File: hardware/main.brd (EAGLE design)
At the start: 96.5 x 65.5 mm, 93 parts, among them SW1 USER_SLIDE, SW2 USER_SLIDE, U1 TMS320F28069_PN_80, U10 TXB0101_DBV_6, U2 SN74LVC4245A_DW_24, U3 Value, U4 SN74LVC4245A_DW_24, U5 Value, U6 SN74ABT541B_DW_20, U7 SN74LVC1G04_DBV_5, U8 SST25VF080BS2AF, U9 TXB0101_DBV_6

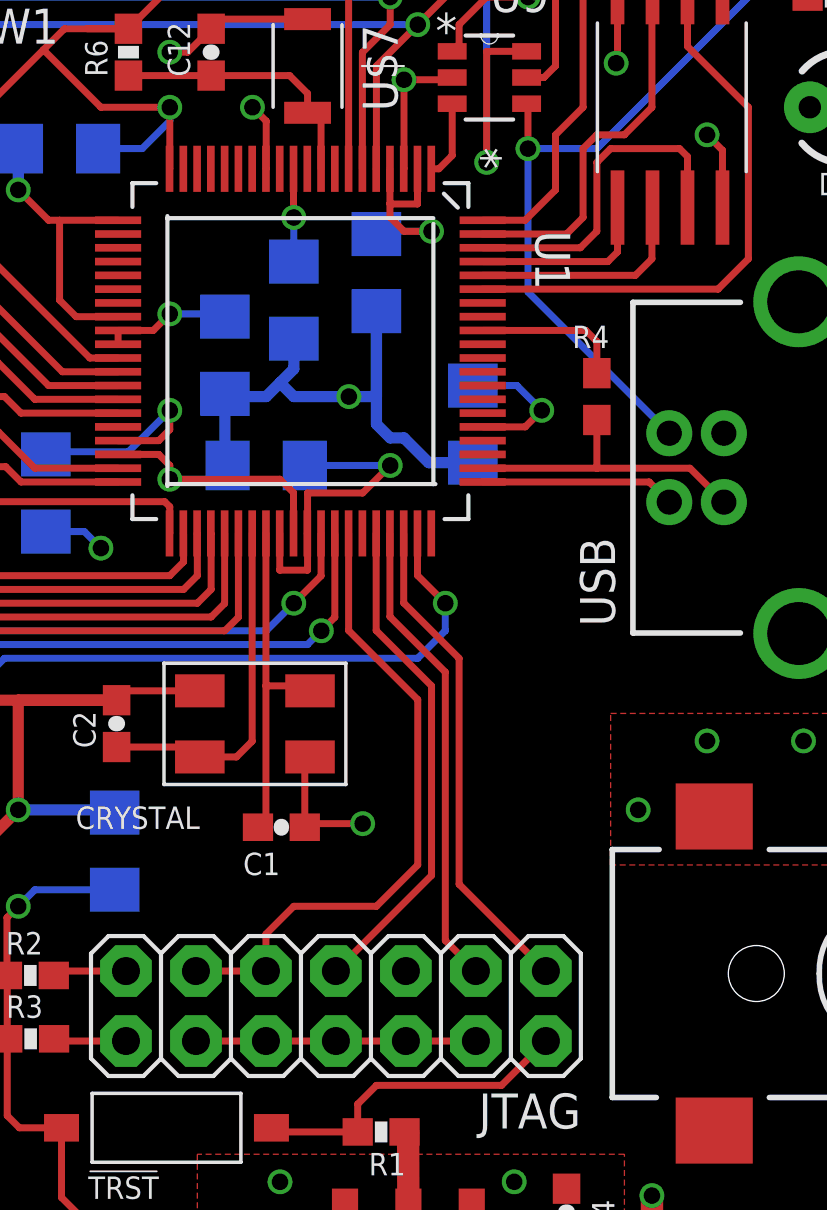
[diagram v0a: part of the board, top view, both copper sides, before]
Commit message: Fixed minor error with JTAG. TRST pin not connected
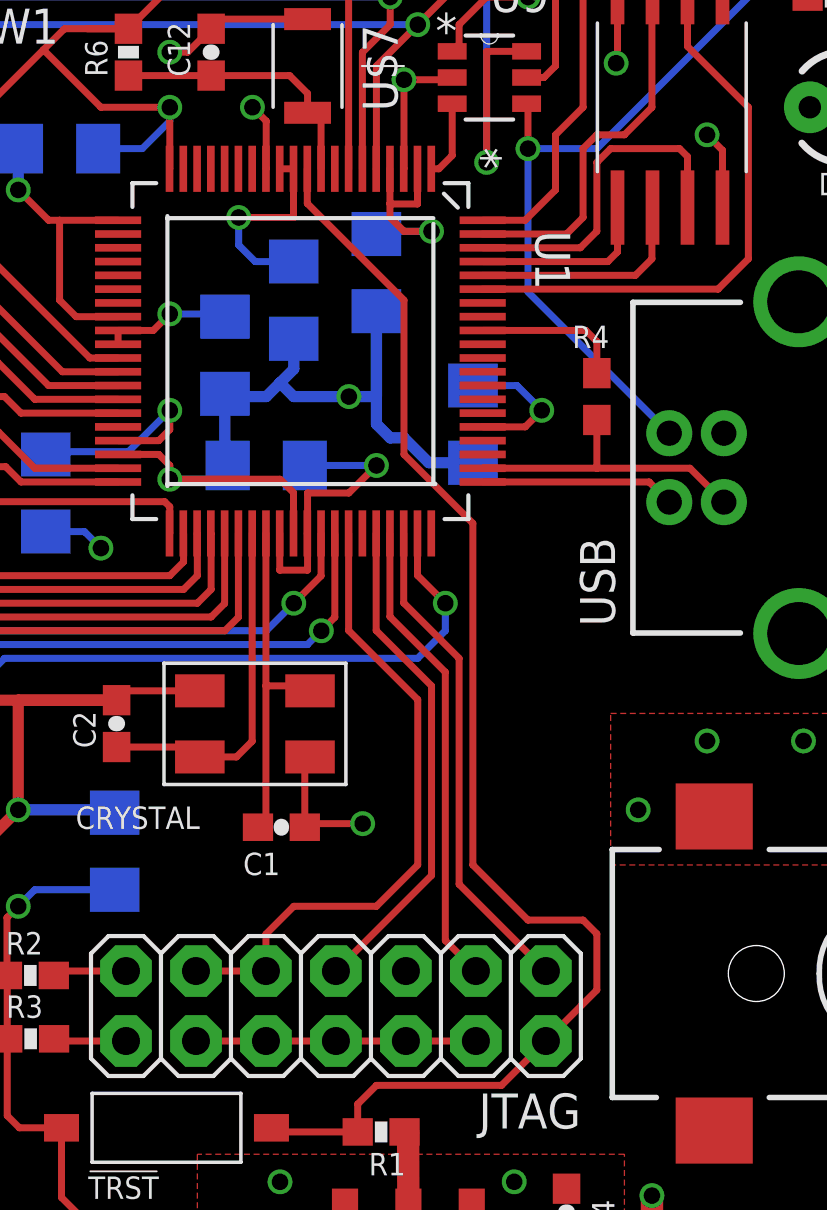
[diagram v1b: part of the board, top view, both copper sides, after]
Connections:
- removed net N$1: !TRST!.P$1, JTAG.2, R1.2
- net !TRST!: now also !TRST!.P$1, JTAG.2, R1.2
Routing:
- net !TRST!: track 0.00 -> 49.9 mm
- net N$1: track 12.0 -> 0.00 mm
- net 3.3V: track 152.2 -> 155.3 mm
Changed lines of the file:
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@@
 <wire x1="69.4" y1="41" x2="69.5" y2="40.9" width="0.254" layer="16"/>
 <wire x1="71.9900125" y1="46.2667" x2="71.9900125" y2="44.5" width="0.254" layer="1"/>
-<wire x1="71.9900125" y1="44.5" x2="72" y2="44.5" width="0.254" layer="1"/>
-<via x="72" y="44.5" extent="1-16" drill="0.6"/>
-<wire x1="72" y1="44.5" x2="72" y2="42.9" width="0.254" layer="16"/>
+<wire x1="71.9900125" y1="44.5" x2="70" y2="44.5" width="0.254" layer="1"/>
+<via x="70" y="44.5" extent="1-16" drill="0.6"/>
 <wire x1="75.49000625" y1="46.2667" x2="75.49000625" y2="45" width="0.254" layer="1"/>
 <wire x1="75.49000625" y1="45" x2="75.49000625" y2="44.50999375" width="0.254" layer="1"/>
@@
 <wire x1="81" y1="37.5" x2="80.1" y2="38.4" width="0.254" layer="16"/>
 <wire x1="80.1" y1="38.4" x2="78.5" y2="38.4" width="0.254" layer="16"/>
-<wire x1="72.5" y1="34.5" x2="74.5" y2="34.5" width="0.254" layer="1"/>
-<wire x1="74.5" y1="34.5" x2="75.5" y2="35.5" width="0.254" layer="1"/>
-<via x="75.5" y="35.5" extent="1-16" drill="0.6"/>
-<wire x1="75.5" y1="35.5" x2="72.4" y2="35.5" width="0.254" layer="16"/>
+<wire x1="72.5" y1="34.5" x2="74" y2="34.5" width="0.254" layer="1"/>
+<wire x1="74" y1="34.5" x2="75" y2="35.5" width="0.254" layer="1"/>
+<via x="75" y="35.5" extent="1-16" drill="0.6"/>
+<wire x1="75" y1="35.5" x2="72.4" y2="35.5" width="0.254" layer="16"/>
 <wire x1="72.4899875" y1="33.0333" x2="72.5" y2="33.0433125" width="0.254" layer="1"/>
 <wire x1="72.5" y1="33.0433125" x2="72.5" y2="34.5" width="0.254" layer="1"/>
@@
 <wire x1="78.8567" y1="40.4000125" x2="78.8567" y2="41.400009375" width="0" layer="19" extent="1-1"/>
 <wire x1="78.5" y1="38.4" x2="78.8567" y2="40.4000125" width="0" layer="19" extent="1-16"/>
-<wire x1="71.4899875" y1="46.2667" x2="71.9900125" y2="46.2667" width="0" layer="19" extent="1-1"/>
 <wire x1="78.8567" y1="35.89999375" x2="78.8567" y2="36.89999375" width="0" layer="19" extent="1-1"/>
+<wire x1="71.4899875" y1="46.2667" x2="71.9900125" y2="46.2667" width="0.254" layer="1"/>
+<wire x1="72" y1="42.9" x2="70.6" y2="42.9" width="0.254" layer="16"/>
+<wire x1="70.6" y1="42.9" x2="70" y2="43.5" width="0.254" layer="16"/>
+<wire x1="70" y1="43.5" x2="70" y2="44.5" width="0.254" layer="16"/>
 </signal>
 <signal name="GND">
@@
 <signal name="!TRST!">
 <contactref element="U1" pad="10"/>
+<contactref element="JTAG" pad="2"/>
+<contactref element="!TRST!" pad="P$1"/>
+<contactref element="R1" pad="2"/>
+<wire x1="71.19" y1="11.46" x2="71.34" y2="11.31" width="0.254" layer="1"/>
+<wire x1="71.34" y1="11.31" x2="74.32" y2="11.31" width="0.254" layer="1"/>
+<wire x1="81.15" y1="14.61" x2="79.54" y2="13" width="0.254" layer="1"/>
+<wire x1="79.54" y1="13" x2="75" y2="13" width="0.254" layer="1"/>
+<wire x1="75" y1="13" x2="74.32" y2="12.32" width="0.254" layer="1"/>
+<wire x1="74.32" y1="12.32" x2="74.32" y2="11.31" width="0.254" layer="1"/>
+<wire x1="72.4899875" y1="46.2667" x2="72.4899875" y2="45.0100125" width="0.254" layer="1"/>
+<wire x1="72.4899875" y1="45.0100125" x2="76" y2="41.5" width="0.254" layer="1"/>
+<wire x1="76" y1="41.5" x2="76" y2="35.9" width="0.254" layer="1"/>
+<wire x1="78.5" y1="21" x2="78.5" y2="33.4" width="0.254" layer="1"/>
+<wire x1="78.5" y1="33.4" x2="76" y2="35.9" width="0.254" layer="1"/>
+<wire x1="78.5" y1="21" x2="80.5" y2="19" width="0.254" layer="1"/>
+<wire x1="80.5" y1="19" x2="82.5" y2="19" width="0.254" layer="1"/>
+<wire x1="82.5" y1="19" x2="83" y2="18.5" width="0.254" layer="1"/>
+<wire x1="83" y1="18.5" x2="83" y2="16.46" width="0.254" layer="1"/>
+<wire x1="83" y1="16.46" x2="81.15" y2="14.61" width="0.254" layer="1"/>
 </signal>
 <signal name="X1">
@@
 <wire x1="71.1496" y1="61.7004" x2="75.5" y2="61.7004" width="0.254" layer="1"/>
 </signal>
-<signal name="N$1">
-<contactref element="JTAG" pad="2"/>
-<contactref element="!TRST!" pad="P$1"/>
-<contactref element="R1" pad="2"/>
-<wire x1="71.19" y1="11.46" x2="71.34" y2="11.31" width="0.254" layer="1"/>
-<wire x1="71.34" y1="11.31" x2="74.32" y2="11.31" width="0.254" layer="1"/>
-<wire x1="81.15" y1="14.61" x2="79.54" y2="13" width="0.254" layer="1"/>
-<wire x1="79.54" y1="13" x2="75" y2="13" width="0.254" layer="1"/>
-<wire x1="75" y1="13" x2="74.32" y2="12.32" width="0.254" layer="1"/>
-<wire x1="74.32" y1="12.32" x2="74.32" y2="11.31" width="0.254" layer="1"/>
-</signal>
 <signal name="N$41">

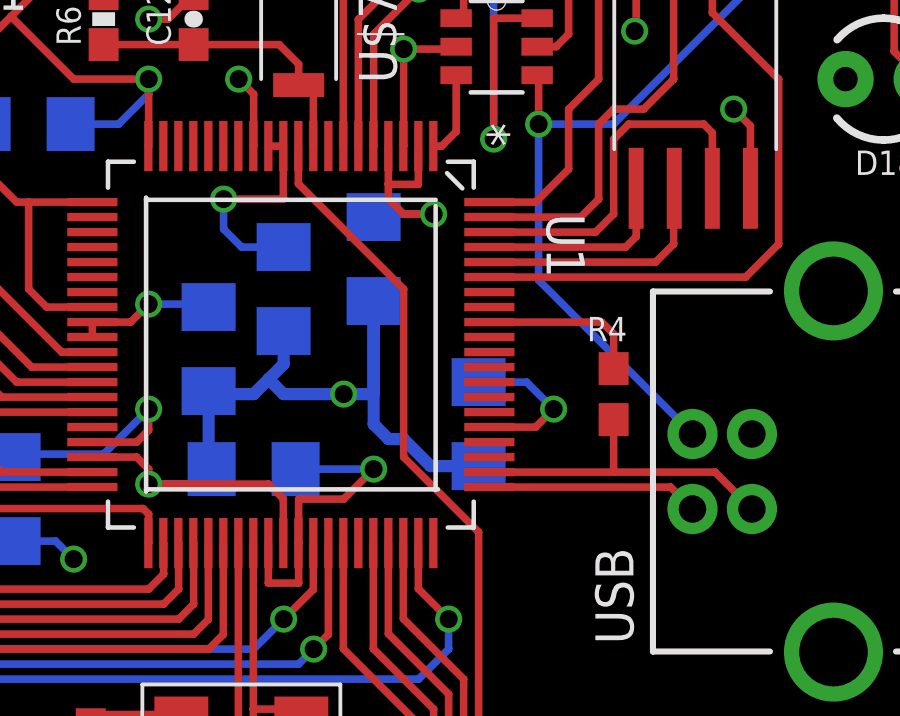
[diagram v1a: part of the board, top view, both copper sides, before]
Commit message: Routed un-noticed airwires. Tried to add SPI breakout. Unsuccessful
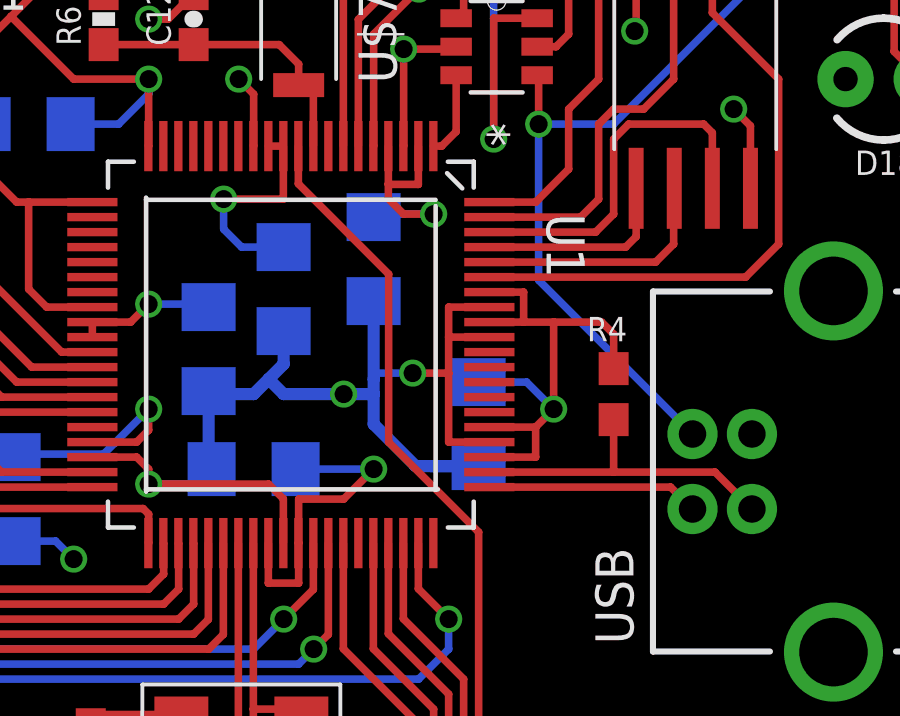
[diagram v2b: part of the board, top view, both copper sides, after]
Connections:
- new net CE1: U1.67
- new net CE2: U1.69
- new net CE3: U1.70
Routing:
- net GND: track 265.0 -> 274.8 mm, vias 28 -> 29
- net 3.3V: track 155.3 -> 162.9 mm
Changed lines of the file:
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@@
 <wire x1="83" y1="38.85" x2="83" y2="40" width="0.254" layer="1"/>
 <wire x1="83" y1="40" x2="82.5999875" y2="40.4000125" width="0.254" layer="1"/>
-<wire x1="82.5999875" y1="40.4000125" x2="78.8567" y2="40.4000125" width="0.254" layer="1"/>
+<wire x1="82.5999875" y1="40.4000125" x2="81" y2="40.4000125" width="0.254" layer="1"/>
+<wire x1="80" y1="40.4000125" x2="78.8567" y2="40.4000125" width="0.254" layer="1"/>
 <wire x1="61.6" y1="14.69" x2="61.6" y2="11.9" width="0.254" layer="1"/>
 <wire x1="61.6" y1="11.9" x2="62.04" y2="11.46" width="0.254" layer="1"/>
@@
 <wire x1="67.09999375" y1="36.39999375" x2="67.5" y2="36.8" width="0.254" layer="1"/>
 <wire x1="67.5" y1="36.8" x2="67.5" y2="37.5" width="0.254" layer="1"/>
-<wire x1="78.8567" y1="40.4000125" x2="78.8567" y2="41.400009375" width="0" layer="19" extent="1-1"/>
-<wire x1="78.5" y1="38.4" x2="78.8567" y2="40.4000125" width="0" layer="19" extent="1-16"/>
-<wire x1="78.8567" y1="35.89999375" x2="78.8567" y2="36.89999375" width="0" layer="19" extent="1-1"/>
 <wire x1="71.4899875" y1="46.2667" x2="71.9900125" y2="46.2667" width="0.254" layer="1"/>
 <wire x1="72" y1="42.9" x2="70.6" y2="42.9" width="0.254" layer="16"/>
 <wire x1="70.6" y1="42.9" x2="70" y2="43.5" width="0.254" layer="16"/>
 <wire x1="70" y1="43.5" x2="70" y2="44.5" width="0.254" layer="16"/>
+<wire x1="78.8567" y1="35.89999375" x2="80.39999375" y2="35.89999375" width="0.254" layer="1"/>
+<wire x1="80.39999375" y1="35.89999375" x2="80.39999375" y2="36.89999375" width="0.254" layer="1"/>
+<wire x1="78.8567" y1="41.400009375" x2="80" y2="41.400009375" width="0.254" layer="1"/>
+<wire x1="80" y1="41.400009375" x2="80" y2="40.4000125" width="0.254" layer="1"/>
+<wire x1="80" y1="40.4000125" x2="81" y2="40.4000125" width="0.254" layer="1"/>
+<wire x1="81" y1="40.4000125" x2="81" y2="37.5" width="0.254" layer="1"/>
 </signal>
 <signal name="GND">
@@
 <wire x1="69.6" y1="38" x2="71" y2="38" width="0.4064" layer="16"/>
 <wire x1="71" y1="38" x2="71.5" y2="38.5" width="0.4064" layer="16"/>
-<wire x1="75" y1="41.1" x2="75" y2="37" width="0.4064" layer="16"/>
-<wire x1="75" y1="37" x2="75.5" y2="36.5" width="0.4064" layer="16"/>
-<wire x1="75.5" y1="36.5" x2="76" y2="36.5" width="0.4064" layer="16"/>
-<wire x1="76" y1="36.5" x2="76.9" y2="35.6" width="0.4064" layer="16"/>
-<wire x1="76.9" y1="35.6" x2="78.5" y2="35.6" width="0.4064" layer="16"/>
+<wire x1="75" y1="38" x2="75" y2="37" width="0.4064" layer="16"/>
+<wire x1="76.4" y1="35.6" x2="78.5" y2="35.6" width="0.4064" layer="16"/>
 <wire x1="69.6" y1="35.5" x2="69.5" y2="35.6" width="0.4064" layer="16"/>
 <wire x1="69.5" y1="35.6" x2="69.5" y2="38.1" width="0.4064" layer="16"/>
-<wire x1="75" y1="41.1" x2="75" y2="38" width="0.4064" layer="16"/>
+<wire x1="75" y1="41.1" x2="75" y2="38.5" width="0.4064" layer="16"/>
+<wire x1="75" y1="38.5" x2="75" y2="38" width="0.4064" layer="16"/>
 <wire x1="75" y1="38" x2="74" y2="38" width="0.4064" layer="16"/>
 <via x="74" y="38" extent="1-16" drill="0.6"/>
@@
 <wire x1="47.6" y1="39.4" x2="48" y2="39" width="0.254" layer="16"/>
 <wire x1="48" y1="39" x2="48" y2="34.5" width="0.254" layer="16"/>
-<wire x1="78.8567" y1="39.8999875" x2="78.8567" y2="40.900009375" width="0" layer="19" extent="1-1"/>
-<wire x1="78.8567" y1="36.39999375" x2="78.8567" y2="39.8999875" width="0" layer="19" extent="1-1"/>
-<wire x1="78.5" y1="35.6" x2="78.8567" y2="36.39999375" width="0" layer="19" extent="1-16"/>
+<wire x1="78.8567" y1="40.900009375" x2="77.5" y2="40.900009375" width="0.254" layer="1"/>
+<wire x1="77.5" y1="40.900009375" x2="77.5" y2="39.8999875" width="0.254" layer="1"/>
+<wire x1="77.5" y1="39.8999875" x2="77.5" y2="38.7" width="0.254" layer="1"/>
+<wire x1="77.5" y1="38.7" x2="77.5" y2="36.39999375" width="0.254" layer="1"/>
+<wire x1="77.5" y1="36.39999375" x2="78.8567" y2="36.39999375" width="0.254" layer="1"/>
+<wire x1="78.8567" y1="39.8999875" x2="77.5" y2="39.8999875" width="0.254" layer="1"/>
+<wire x1="78.5" y1="35.6" x2="76.9" y2="35.6" width="0.4064" layer="16"/>
+<wire x1="76.4" y1="35.6" x2="75" y2="37" width="0.4064" layer="16"/>
+<via x="76.3" y="38.7" extent="1-16" drill="0.6"/>
+<wire x1="76.3" y1="38.7" x2="77.5" y2="38.7" width="0.254" layer="1"/>
+<wire x1="76.3" y1="38.7" x2="75" y2="38.7" width="0.254" layer="16"/>
+<wire x1="75" y1="38.7" x2="75" y2="38.5" width="0.254" layer="16"/>
 </signal>
 <signal name="TDI">
@@
 <wire x1="74.32" y1="12.32" x2="74.32" y2="11.31" width="0.254" layer="1"/>
 <wire x1="72.4899875" y1="46.2667" x2="72.4899875" y2="45.0100125" width="0.254" layer="1"/>
-<wire x1="72.4899875" y1="45.0100125" x2="76" y2="41.5" width="0.254" layer="1"/>
-<wire x1="76" y1="41.5" x2="76" y2="35.9" width="0.254" layer="1"/>
+<wire x1="72.4899875" y1="45.0100125" x2="75.5" y2="42" width="0.254" layer="1"/>
+<wire x1="75.5" y1="42" x2="75.5" y2="36.4" width="0.254" layer="1"/>
 <wire x1="78.5" y1="21" x2="78.5" y2="33.4" width="0.254" layer="1"/>
-<wire x1="78.5" y1="33.4" x2="76" y2="35.9" width="0.254" layer="1"/>
+<wire x1="78.5" y1="33.4" x2="75.5" y2="36.4" width="0.254" layer="1"/>
 <wire x1="78.5" y1="21" x2="80.5" y2="19" width="0.254" layer="1"/>
 <wire x1="80.5" y1="19" x2="82.5" y2="19" width="0.254" layer="1"/>
@@
 <wire x1="92.35" y1="49.42" x2="92.35" y2="52.5" width="0.254" layer="1"/>
 </signal>
+<signal name="CE3">
+<contactref element="U1" pad="70"/>
+</signal>
+<signal name="CE2">
+<contactref element="U1" pad="69"/>
+</signal>
+<signal name="CE1">
+<contactref element="U1" pad="67"/>
+</signal>
 </signals>

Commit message: Added SPI breakout. Routed and updated silkscreen for SPI breakout
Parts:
- added JP2: FEMALE 2x3, SparkFun-Connectors:2X3
- moved D18 11.0 mm to (93.0, 59.5)
- moved R37 2.00 mm to (91.5, 54.5)
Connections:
- removed net CE2: U1.69
- removed net CE3: U1.70
- net 3.3V: now also JP2.5
- net CE1: now also JP2.4, U1.60; no longer U1.67
- net GND: now also JP2.6
- net SPICLK: now also JP2.1
- net SPISIMO: now also JP2.2
- net SPISOMI: now also JP2.3
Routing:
- net CE1: track 0.00 -> 36.2 mm, vias 0 -> 1
- net SPISIMO: track 6.65 -> 21.9 mm, vias 0 -> 1
- net SPICLK: track 8.26 -> 18.3 mm, vias 0 -> 1
- net N$2: track 29.3 -> 34.0 mm
- net SPISOMI: track 20.9 -> 24.8 mm
- net !FLASHHOLD!: track 12.4 -> 9.96 mm, vias 0 -> 2
- net N$42: track 4.38 -> 6.47 mm
- net 5V: track 187.4 -> 185.4 mm
- net 3.3V: track 162.9 -> 164.4 mm
- net !FLASHWP!: track 13.9 -> 13.0 mm
